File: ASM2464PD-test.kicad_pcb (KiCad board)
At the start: 4 copper layers, 81.8 x 19 mm, 93 parts, among them J1 USB_C_Receptacle, J10 Conn_01x06, J2 SPIheader, J3 Bus_PCI_Express_x4, J4 chip-annoyers, J5 UART, J6 I2C, J7 Conn_01x06, J8 Conn_01x06, J9 Conn_01x06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

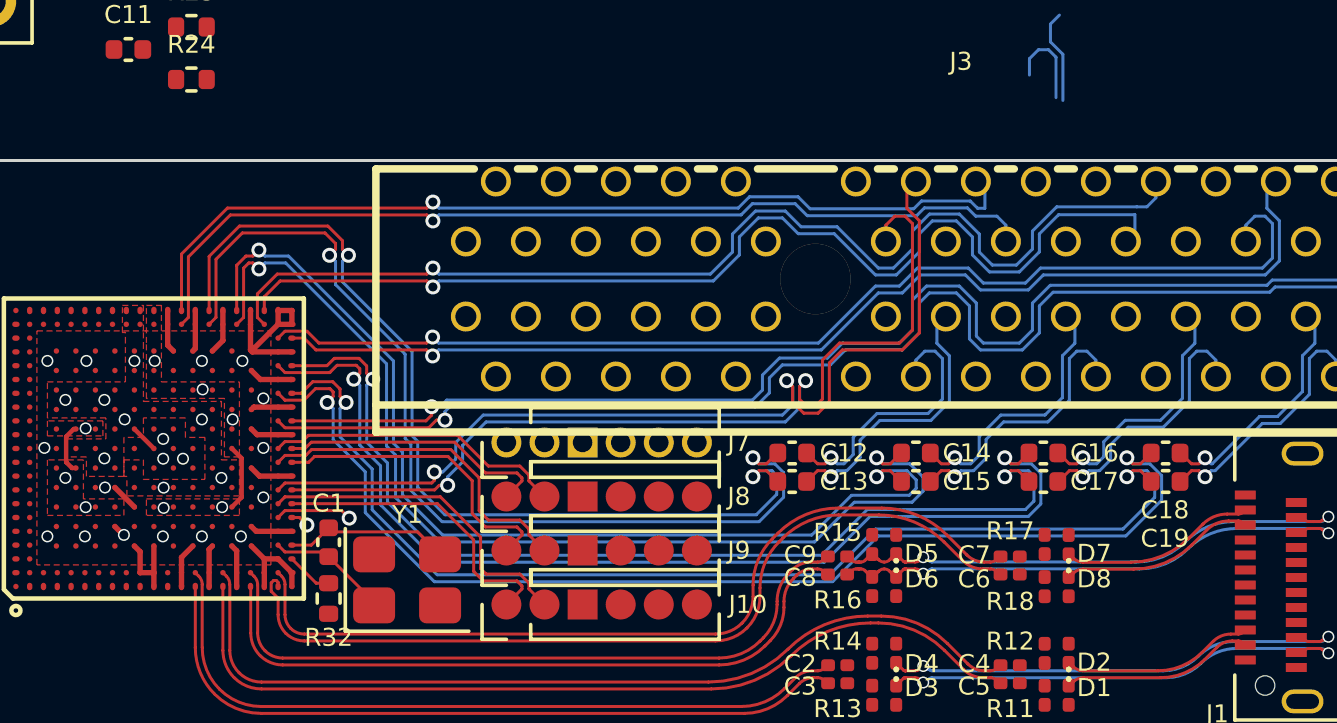
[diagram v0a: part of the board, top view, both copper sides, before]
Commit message: Made some space for future 12V supply trace
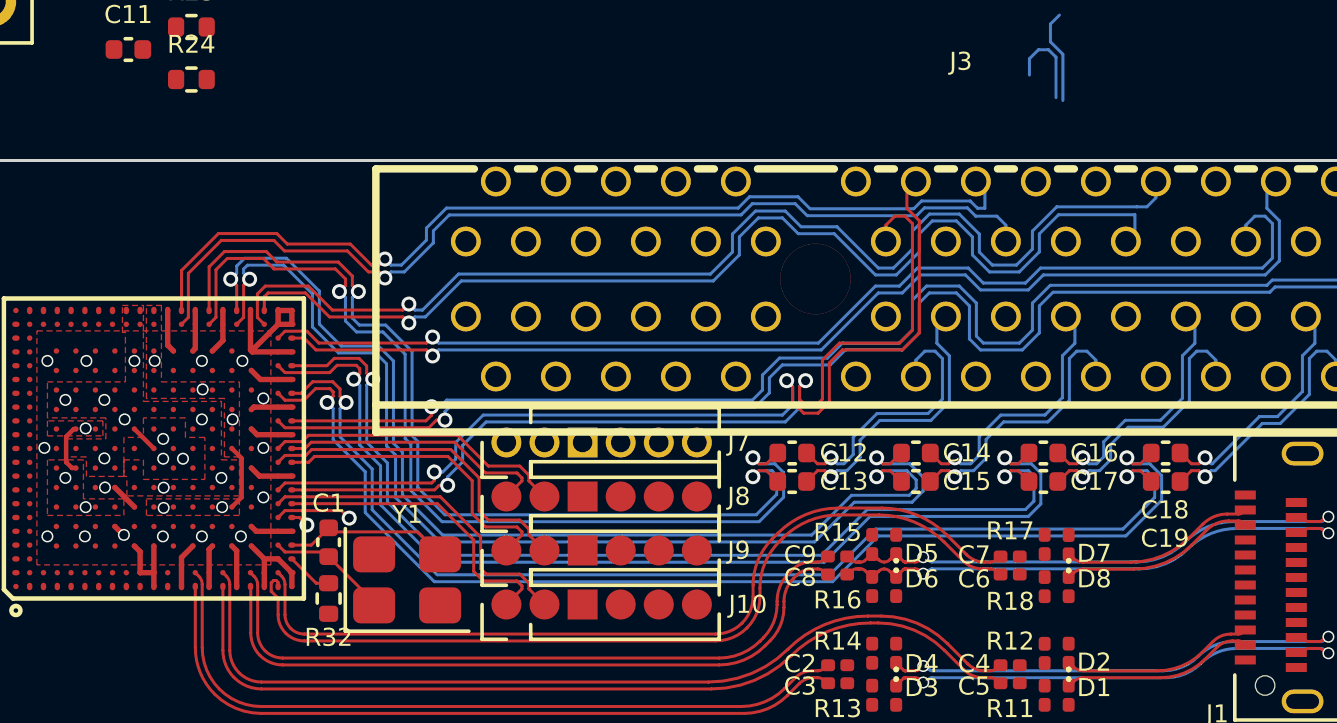
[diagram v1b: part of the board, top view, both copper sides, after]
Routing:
- net PCIe_TX0-: track 31.5 -> 30.7 mm
- net PCIe_TX0+: track 32.5 -> 31.6 mm
- net PCIe_RX0-: track 31.5 -> 32.3 mm
- net PCIe_RX0+: track 31.0 -> 31.8 mm
- net PCIe_RX1-: track 40.6 -> 41.3 mm
- net PCIe_RX1+: track 39.2 -> 39.9 mm
- net PCIe_TX1+: track 35.2 -> 35.7 mm
- net PCIe_TX1-: track 34.2 -> 34.8 mm

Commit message: some notes
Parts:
- moved J1 1.36 mm to (203.8, 98.7)
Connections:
- J7 pad 4: PE_WAKE# -> PERST0#
- J7 pad 5: PERST0# -> CLKREQ0#
- J7 pad 6: CLKREQ0# -> PE_WAKE#
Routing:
- net /Main/URX1_C-: track 6.50 -> 7.86 mm
- net /Main/URX1_C+: track 6.50 -> 7.86 mm
- net /Main/UTX0_C+: track 6.39 -> 7.75 mm
- net /Main/UTX0_C-: track 6.39 -> 7.75 mm
- net /Main/UTX1_C+: track 18.2 -> 19.5 mm
- net /Main/URX0_C+: track 16.1 -> 17.4 mm
- net /Main/UTX1_C-: track 18.2 -> 19.5 mm
- net /Main/URX0_C-: track 16.1 -> 17.4 mm
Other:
- board text added: "Add mount holes"
- board text added: "come up with a cool representation of PCIe gen 4 and put it here"
- board text added: "insert cool art about USB4/TB3 40Gbps here (with lightning)"

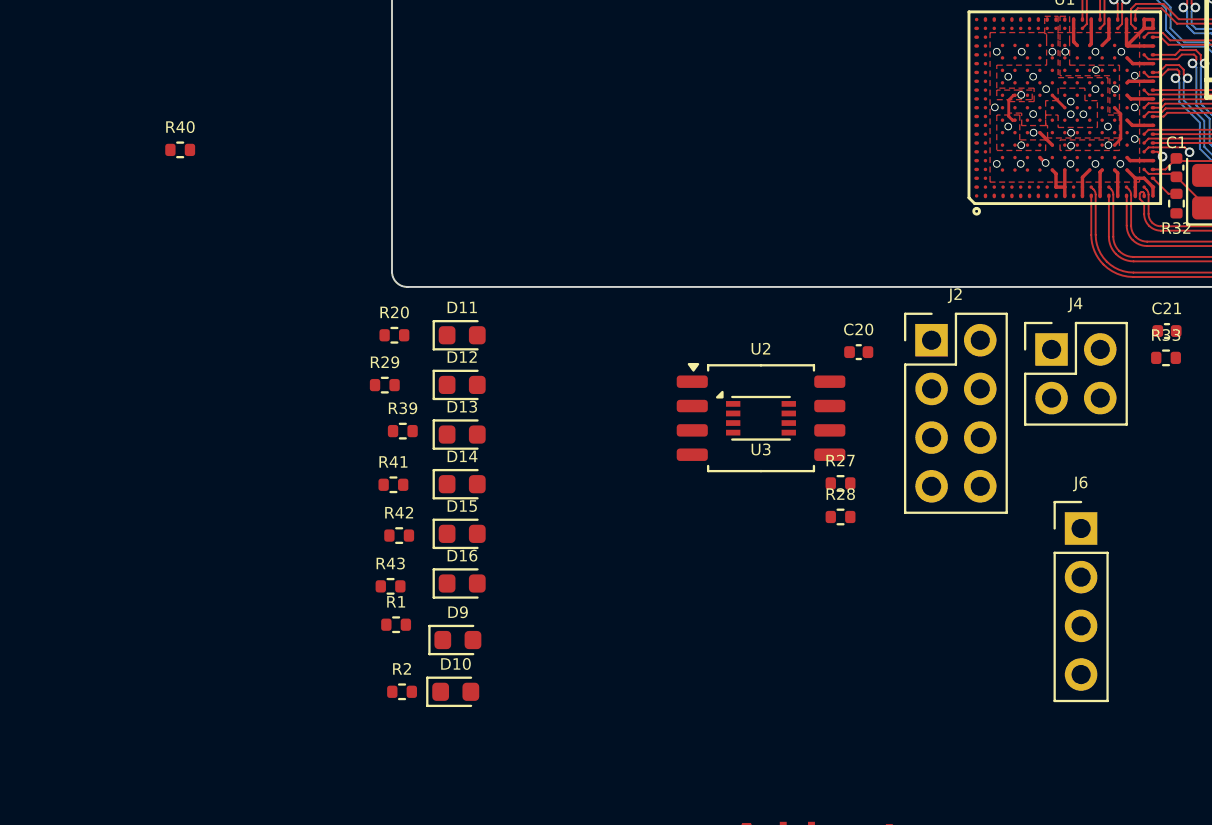
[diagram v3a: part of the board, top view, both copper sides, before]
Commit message: Adjusted fills under asm2464pd a bit
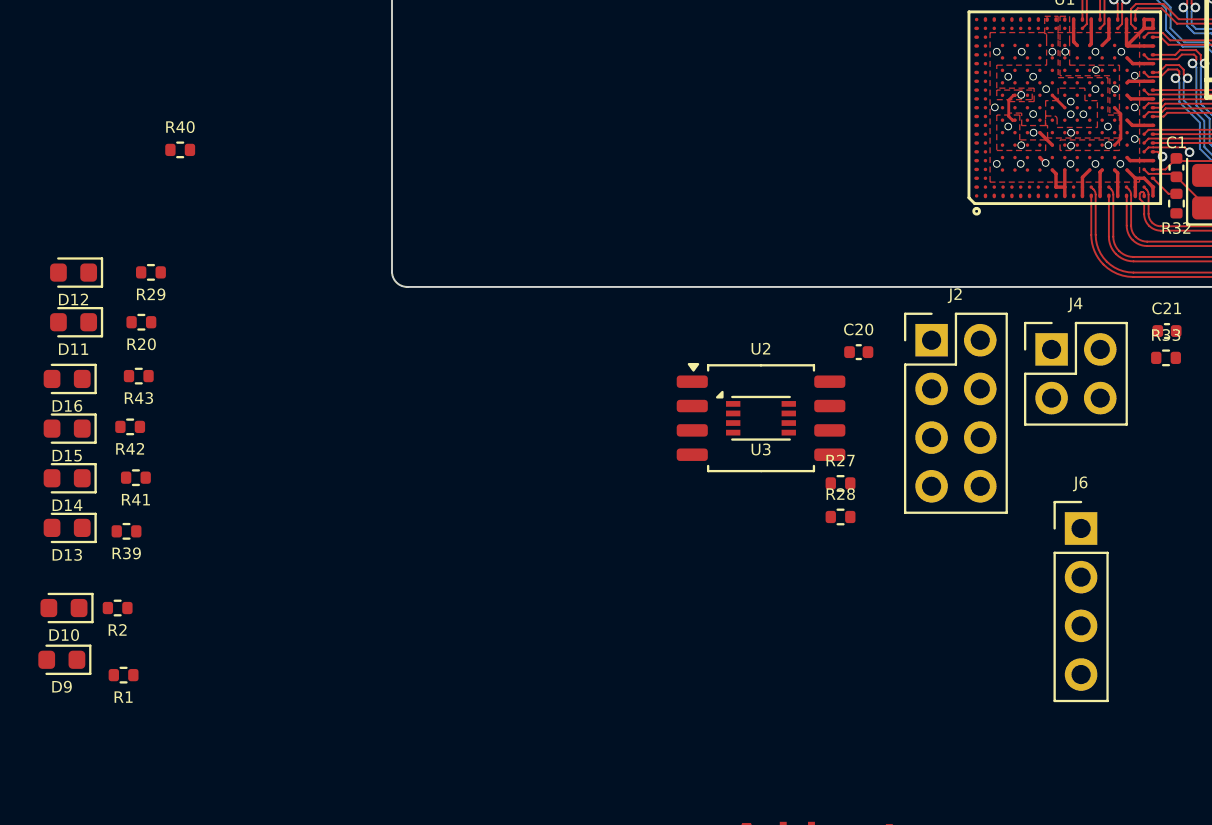
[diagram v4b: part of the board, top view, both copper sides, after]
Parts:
- moved D16 23.2 mm to (109.0, 108.5), turned to 180 degrees
- moved D15 21.3 mm to (109.0, 111.1), turned to 180 degrees
- moved D13 21.2 mm to (109.0, 116.3), turned to 180 degrees
- moved D12 21.1 mm to (109.3, 103.0), turned to 180 degrees
- moved D10 20.9 mm to (108.8, 120.5), turned to 180 degrees
- moved D9 20.7 mm to (108.7, 123.2), turned to 180 degrees
- moved D14 20.6 mm to (109.0, 113.7), turned to 180 degrees
- moved D11 20.3 mm to (109.3, 105.6), turned to 180 degrees
- moved R43 17.1 mm to (112.7, 108.4), turned to 180 degrees
- moved R2 15.5 mm to (111.6, 120.5), turned to 180 degrees
- moved R39 15.3 mm to (112.0, 116.5), turned to 180 degrees
- moved R42 15.1 mm to (112.2, 111.0), turned to 180 degrees
- moved R1 14.5 mm to (111.9, 124.0), turned to 180 degrees
- moved R29 13.5 mm to (113.3, 103.0), turned to 180 degrees
- moved R41 13.4 mm to (112.5, 113.7), turned to 180 degrees
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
